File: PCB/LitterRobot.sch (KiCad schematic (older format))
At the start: 6 parts, among them J1 DF11C-4DP-2V(57), J2 DF11C-6DP-2V(57), J3 DF11C-8DP-2V(57), J4 DF11C-6DP-2V(57)

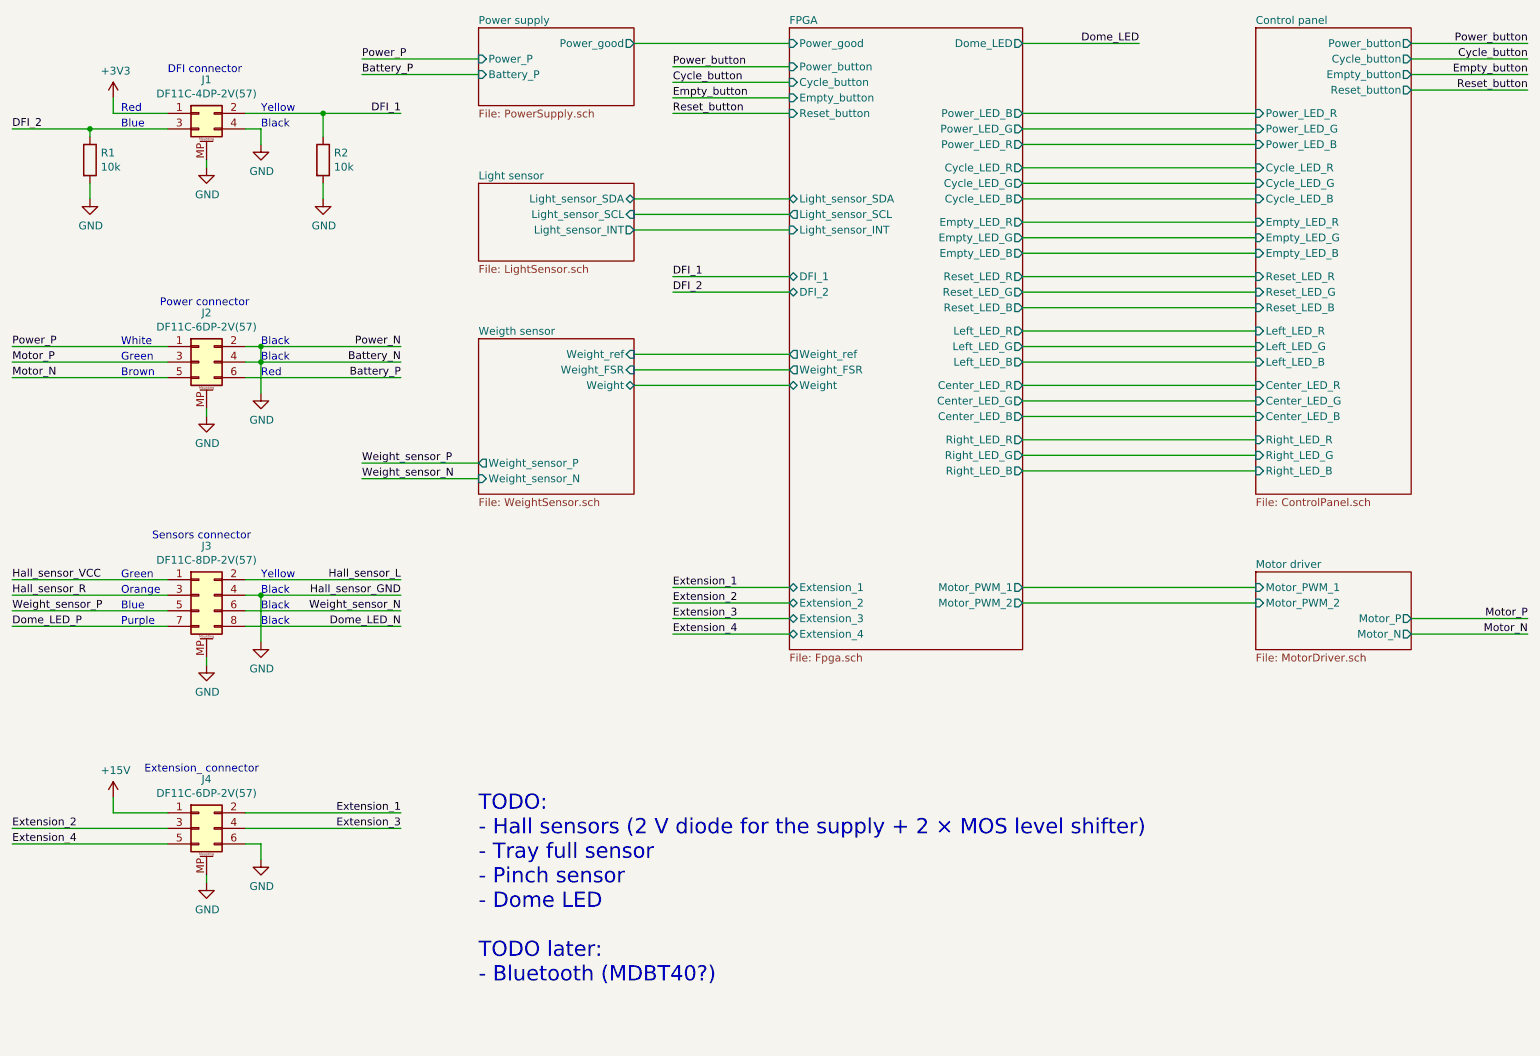
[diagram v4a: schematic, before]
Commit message: Add support for the hall sensors and dome LED
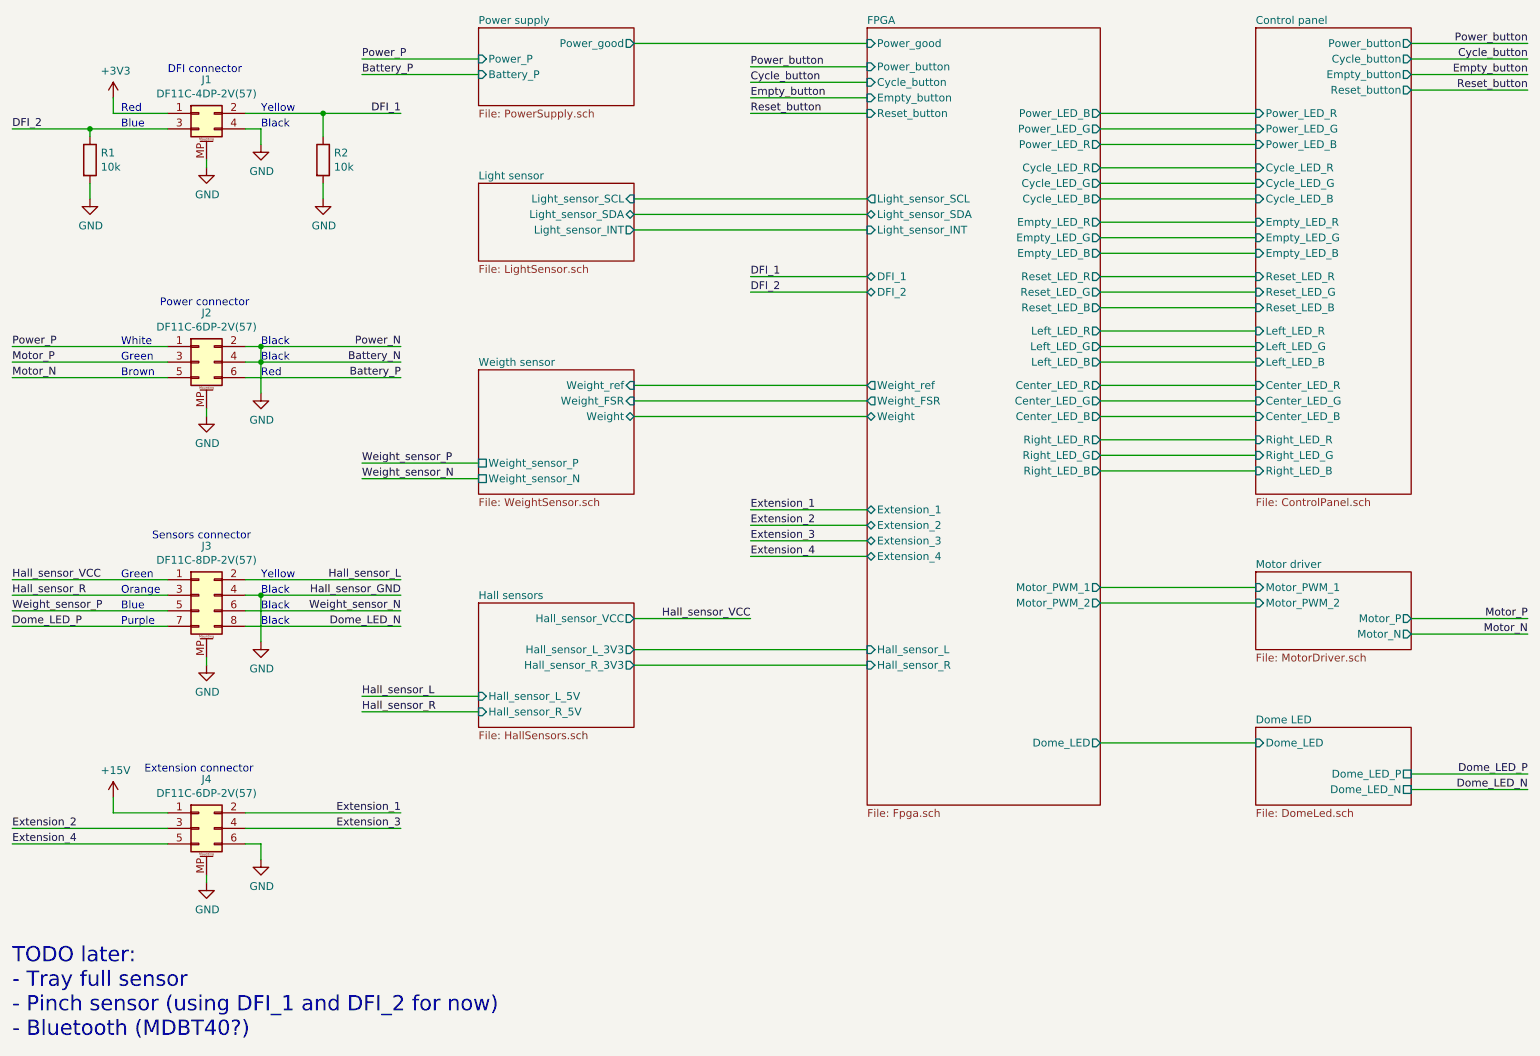
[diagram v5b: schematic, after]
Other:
- note added: "Extension connector"
- note added: "TODO later:\n- Tray full sensor\n- Pinch sensor (using DFI_1 and DFI_2 for now)\n- Bluetooth (MDBT40?)"
- note removed: "Extension_ connector"
- note removed: "TODO:\n- Hall sensors (2 V diode for the supply + 2 × MOS level shifter)\n- Tray full sensor\n- Pinch sensor\n- Dome LED\n\nTODO later:\n- Bluetooth (MDBT40?)"

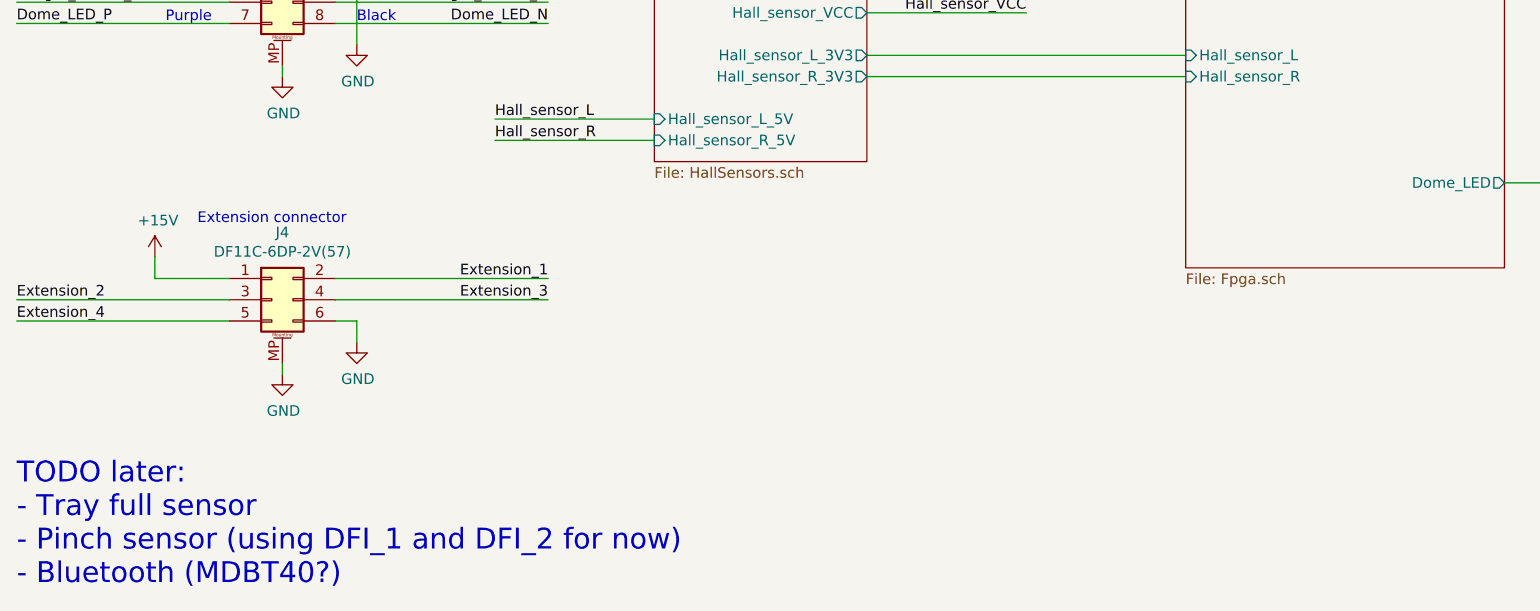
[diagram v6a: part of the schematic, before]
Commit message: Add the EMB1061 Bluetooth module
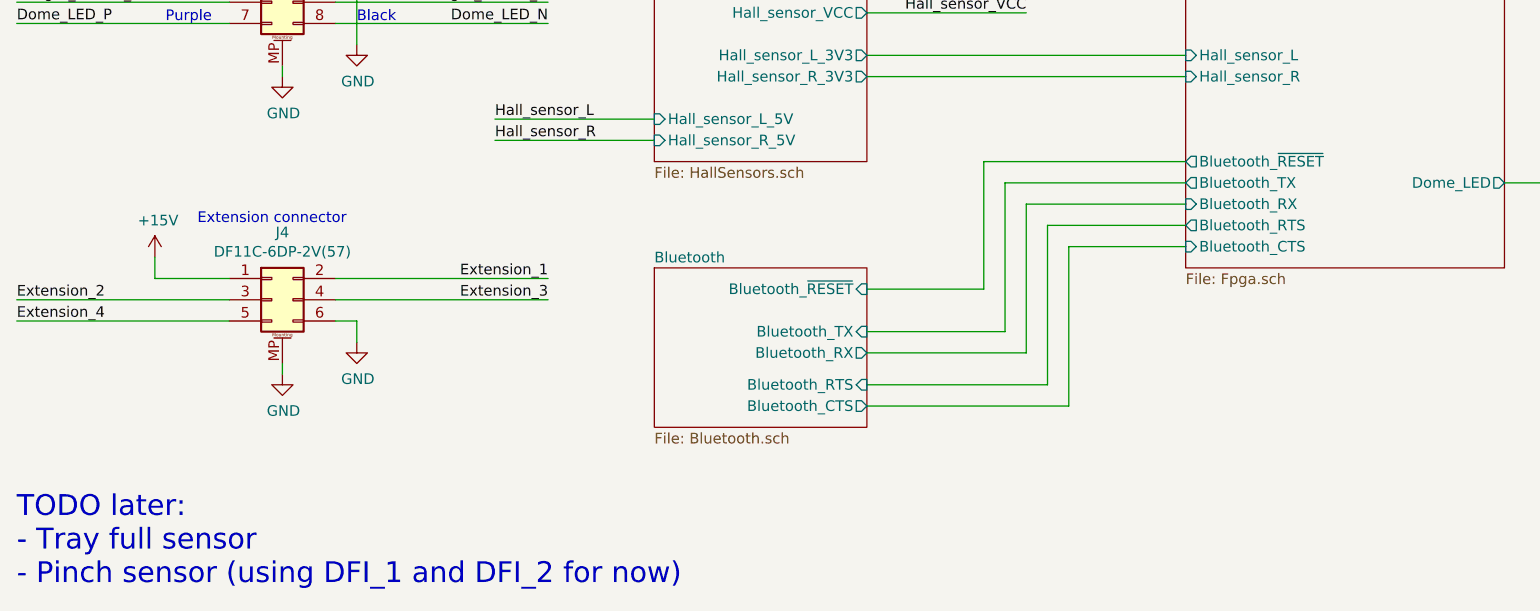
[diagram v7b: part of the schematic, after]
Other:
- note added: "TODO later:\n- Tray full sensor\n- Pinch sensor (using DFI_1 and DFI_2 for now)"
- note removed: "TODO later:\n- Tray full sensor\n- Pinch sensor (using DFI_1 and DFI_2 for now)\n- Bluetooth (MDBT40?)"
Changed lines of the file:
@@
 $Descr A4 11693 8268
 encoding utf-8
-Sheet 1 22
+Sheet 1 23
 Title "Litter Robot 3 - Main board"
-Date "2021-04-05"
+Date "2021-04-10"
 Rev "A1"
 Comp "L. Sartory"
@@
 F43 "Hall_sensor_L" I L 6500 5000 50
 F44 "Hall_sensor_R" I L 6500 5100 50
+F45 "Bluetooth_TX" O L 6500 5600 50
+F46 "Bluetooth_RX" I L 6500 5700 50
+F47 "Bluetooth_CTS" I L 6500 5900 50
+F48 "Bluetooth_RTS" O L 6500 5800 50
+F49 "Bluetooth_~RESET" O L 6500 5500 50
+$EndSheet
+$Sheet
+S 4000 6000 1000 750
+U 606DAA99
+F0 "Bluetooth" 50
+F1 "Bluetooth.sch" 50
+F2 "Bluetooth_TX" I R 5000 6300 50
+F3 "Bluetooth_RX" O R 5000 6400 50
+F4 "Bluetooth_CTS" O R 5000 6650 50
+F5 "Bluetooth_RTS" I R 5000 6550 50
+F6 "Bluetooth_~RESET" I R 5000 6100 50
 $EndSheet
 $Sheet
@@
 DFI_1
 Text Notes 1000 7500 0    98   ~ 0
-TODO later:\n- Tray full sensor\n- Pinch sensor (using DFI_1 and DFI_2 for now)\n- Bluetooth (MDBT40?)
+TODO later:\n- Tray full sensor\n- Pinch sensor (using DFI_1 and DFI_2 for now)
 Text Label 1000 4850 0    50   ~ 0
 Dome_LED_P
@@
 Wire Wire Line
 	10000 5800 10750 5800
+Wire Wire Line
+	5000 6100 5550 6100
+Wire Wire Line
+	5550 6100 5550 5500
+Wire Wire Line
+	5550 5500 6500 5500
+Wire Wire Line
+	5000 6300 5650 6300
+Wire Wire Line
+	5650 6300 5650 5600
+Wire Wire Line
+	5650 5600 6500 5600
+Wire Wire Line
+	6500 5700 5750 5700
+Wire Wire Line
+	5750 5700 5750 6400
+Wire Wire Line
+	5750 6400 5000 6400
+Wire Wire Line
+	5000 6550 5850 6550
+Wire Wire Line
+	5850 6550 5850 5800
+Wire Wire Line
+	5850 5800 6500 5800
+Wire Wire Line
+	6500 5900 5950 5900
+Wire Wire Line
+	5950 5900 5950 6650
+Wire Wire Line
+	5950 6650 5000 6650
 $EndSCHEMATC

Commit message: Connect the Bluetooth module to the FPGA
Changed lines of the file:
@@
 F45 "Bluetooth_TX" O L 6500 5600 50
 F46 "Bluetooth_RX" I L 6500 5700 50
-F47 "Bluetooth_CTS" I L 6500 5900 50
-F48 "Bluetooth_RTS" O L 6500 5800 50
+F47 "Bluetooth_~CTS" I L 6500 5900 50
+F48 "Bluetooth_~RTS" O L 6500 5800 50
 F49 "Bluetooth_~RESET" O L 6500 5500 50
 $EndSheet
@@
 F2 "Bluetooth_TX" I R 5000 6300 50
 F3 "Bluetooth_RX" O R 5000 6400 50
-F4 "Bluetooth_CTS" O R 5000 6650 50
-F5 "Bluetooth_RTS" I R 5000 6550 50
-F6 "Bluetooth_~RESET" I R 5000 6100 50
+F4 "Bluetooth_~RESET" I R 5000 6100 50
+F5 "Bluetooth_~CTS" O R 5000 6650 50
+F6 "Bluetooth_~RTS" I R 5000 6550 50
 $EndSheet
 $Sheet
